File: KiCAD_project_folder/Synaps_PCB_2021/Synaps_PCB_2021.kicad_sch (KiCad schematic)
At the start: 0 parts

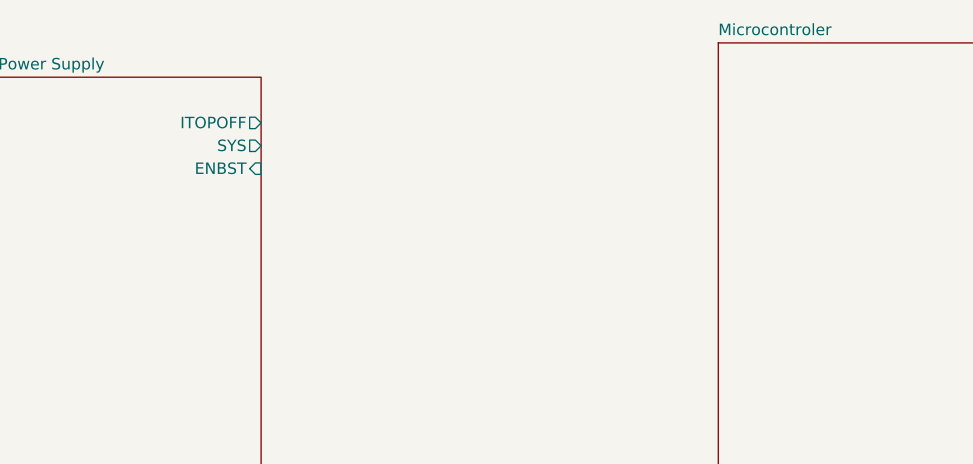
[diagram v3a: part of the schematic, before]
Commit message: Reworking Powersupply
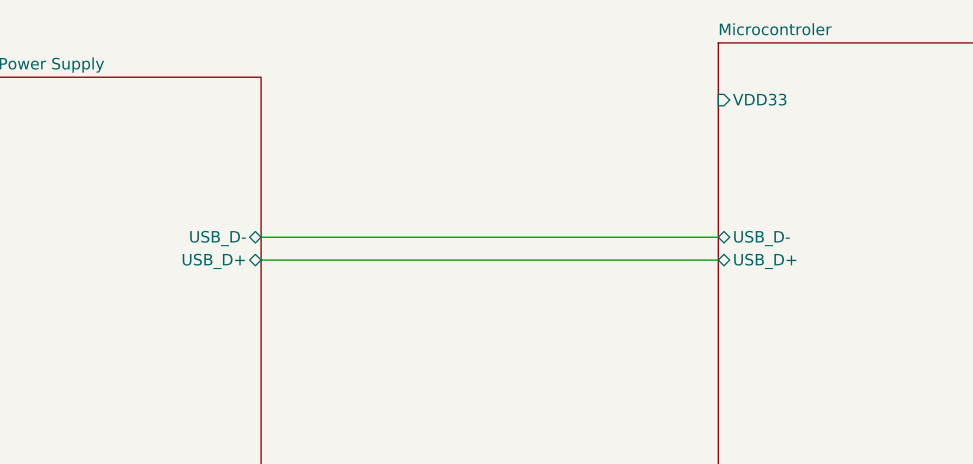
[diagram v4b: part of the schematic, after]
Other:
- sheet Microcontroler ports: added USB_D+, USB_D-, VDD33; removed none
- sheet Power Supply ports: added USB_D+, USB_D-; removed ENBST, ITOPOFF, SYS
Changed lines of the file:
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@@
     (date "2020-12-29")
+  )
+  (wire (pts (xy 76.2 62.23) (xy 127 62.23))
+    (stroke (width 0) (type default) (color 0 0 0 0))
+  )
+  (wire (pts (xy 76.2 59.69) (xy 127 59.69))
+    (stroke (width 0) (type default) (color 0 0 0 0))
   )
   (sheet (at 46.99 41.91) (size 29.21 72.39) (fields_autoplaced)
@@
       (effects (font (size 1.27 1.27)) (justify left top))
     )
-    (pin "ITOPOFF" output (at 76.2 46.99 0)
+    (pin "USB_D-" bidirectional (at 76.2 59.69 0)
       (effects (font (size 1.27 1.27)) (justify right))
     )
-    (pin "SYS" output (at 76.2 49.53 0)
-      (effects (font (size 1.27 1.27)) (justify right))
-    )
-    (pin "ENBST" input (at 76.2 52.07 0)
+    (pin "USB_D+" bidirectional (at 76.2 62.23 0)
       (effects (font (size 1.27 1.27)) (justify right))
     )
@@
     (property "Sheet file" "microcontroler.kicad_sch" (id 1) (at 127 114.8846 0)
       (effects (font (size 1.27 1.27)) (justify left top))
+    )
+    (pin "VDD33" input (at 127 44.45 180)
+      (effects (font (size 1.27 1.27)) (justify left))
+    )
+    (pin "USB_D-" bidirectional (at 127 59.69 180)
+      (effects (font (size 1.27 1.27)) (justify left))
+    )
+    (pin "USB_D+" bidirectional (at 127 62.23 180)
+      (effects (font (size 1.27 1.27)) (justify left))
     )
   )
@@
       (reference "#PWR012") (unit 1) (value "VIO") (footprint "")
     )
-    (path "/00000000-0000-0000-0000-0000604af200/ad0e8a75-3c18-4b68-b709-f2c4f54d4827"
-      (reference "#PWR013") (unit 1) (value "VIO") (footprint "")
-    )
     (path "/00000000-0000-0000-0000-0000604b51e6/00000000-0000-0000-0000-000060abb037/acdf1401-7333-43d7-ac3f-2245baffa6ea/43ac6ffa-7b63-4fc0-b2b8-4c9c5eb4bd58"
       (reference "#PWR016") (unit 1) (value "GNDREF") (footprint "")
@@
       (reference "#PWR0102") (unit 1) (value "GNDREF") (footprint "")
     )
-    (path "/00000000-0000-0000-0000-0000604af200/89827649-befc-4750-a34c-13cfb14ed735"
-      (reference "#PWR0103") (unit 1) (value "VIO") (footprint "")
-    )
     (path "/00000000-0000-0000-0000-0000604af200/29ab8ef7-d469-4192-a436-a1a2c51aa419"
       (reference "#PWR0104") (unit 1) (value "GNDREF") (footprint "")
     )
-    (path "/00000000-0000-0000-0000-0000604af200/d9362226-eaaf-4ec2-bc9f-ba927022fb72"
-      (reference "#PWR0105") (unit 1) (value "VIO") (footprint "")
-    )
-    (path "/00000000-0000-0000-0000-0000604af200/9541e854-c63a-412b-a034-49b741e570c2"
-      (reference "#PWR0106") (unit 1) (value "VIO") (footprint "")
+    (path "/00000000-0000-0000-0000-0000604af200/029525a0-8a41-486f-a02b-f13993394b49"
+      (reference "#PWR?") (unit 1) (value "GNDREF") (footprint "")
+    )
+    (path "/00000000-0000-0000-0000-0000604af200/0612be0e-3ae0-4e28-936e-756a5afc4dbe"
+      (reference "#PWR?") (unit 1) (value "+3.3V") (footprint "")
+    )
+    (path "/00000000-0000-0000-0000-0000604af200/28f76b07-ad8a-4c48-9d57-49c6c6ca56bd"
+      (reference "#PWR?") (unit 1) (value "GNDREF") (footprint "")
+    )
+    (path "/00000000-0000-0000-0000-0000604af200/4ac4cde6-c5b2-4ee8-aa21-e81b8b7c6e89"
+      (reference "#PWR?") (unit 1) (value "GNDREF") (footprint "")
+    )
+    (path "/00000000-0000-0000-0000-0000604af200/6096ff1a-efad-4c96-91e5-2b8353c01857"
+      (reference "#PWR?") (unit 1) (value "GNDREF") (footprint "")
+    )
+    (path "/00000000-0000-0000-0000-0000604af200/75e6a19c-b364-4d0b-97b2-9a6594dafad5"
+      (reference "#PWR?") (unit 1) (value "VAA") (footprint "")
+    )
+    (path "/00000000-0000-0000-0000-0000604af200/8d41ddfc-b02c-4f6e-ad73-25b463ae002b"
+      (reference "#PWR?") (unit 1) (value "GNDREF") (footprint "")
+    )
+    (path "/00000000-0000-0000-0000-0000604af200/b5aba46c-977a-4706-899d-5875980faab4"
+      (reference "#PWR?") (unit 1) (value "VDD") (footprint "")
+    )
+    (path "/00000000-0000-0000-0000-0000604af200/c3897589-3648-454c-9d3d-6573d66fd15c"
+      (reference "#PWR?") (unit 1) (value "GNDREF") (footprint "")
+    )
+    (path "/00000000-0000-0000-0000-0000604af200/e5318905-4b1b-43c9-aa4d-40970fcef07a"
+      (reference "#PWR?") (unit 1) (value "VIO") (footprint "")
+    )
+    (path "/00000000-0000-0000-0000-0000604af200/ef1da815-5ae9-4f7a-859c-d7960e6acc1e"
+      (reference "#PWR?") (unit 1) (value "VBUS") (footprint "")
     )
     (path "/00000000-0000-0000-0000-0000604b2e86/dab29796-d6b3-4d2d-805f-0b5d2109d9de"
@@
       (reference "C63") (unit 1) (value "10nF/6.3V(10%)") (footprint "Capacitor_SMD:C_1206_3216Metric_Pad1.33x1.80mm_HandSolder")
     )
+    (path "/00000000-0000-0000-0000-0000604af200/afa1e3e3-9a93-4a9d-be10-b6a15433e600"
+      (reference "C?") (unit 1) (value "0.1uF") (footprint "")
+    )
+    (path "/00000000-0000-0000-0000-0000604af200/b68089f8-3576-4418-ba7c-a83d273f4433"
+      (reference "C?") (unit 1) (value "10uF") (footprint "")
+    )
+    (path "/00000000-0000-0000-0000-0000604af200/e5285c42-bd99-4599-82cc-7692ec105054"
+      (reference "C?") (unit 1) (value "0.1uF") (footprint "")
+    )
+    (path "/00000000-0000-0000-0000-0000604af200/f6629c18-4df5-48ea-99b2-c77713f98e19"
+      (reference "C?") (unit 1) (value "10uF") (footprint "")
+    )
     (path "/00000000-0000-0000-0000-0000604af200/5213bc81-6974-4343-aba7-970b9f36c652"
       (reference "D2") (unit 1) (value "LED") (footprint "LED_SMD:LED_1206_3216Metric_Pad1.42x1.75mm_HandSolder")
@@
       (reference "L4") (unit 1) (value "INDUCTOR") (footprint "Inductor_SMD:L_1206_3216Metric_Pad1.22x1.90mm_HandSolder")
     )
+    (path "/00000000-0000-0000-0000-0000604af200/9d05efa6-c335-40cb-8451-b925832a8438"
+      (reference "L?") (unit 1) (value "L_Ferrite") (footprint "")
+    )
     (path "/00000000-0000-0000-0000-0000604af200/30e58f79-c173-4870-9af4-7e80c241c783"
       (reference "Q2") (unit 1) (value "Q_PMOS_DGS") (footprint "")
@@
       (reference "R2") (unit 1) (value "10K") (footprint "Resistor_SMD:R_1206_3216Metric_Pad1.30x1.75mm_HandSolder")
     )
-    (path "/00000000-0000-0000-0000-0000604af200/6f377bca-1c7b-4d57-a89d-9e25d90f18a5"
-      (reference "R3") (unit 1) (value "4.7K") (footprint "Resistor_SMD:R_1206_3216Metric_Pad1.30x1.75mm_HandSolder")
-    )
-    (path "/00000000-0000-0000-0000-0000604af200/c8d586cf-013f-4922-a958-a02f8fecd9fa"
-      (reference "R4") (unit 1) (value "4.7K") (footprint "Resistor_SMD:R_1206_3216Metric_Pad1.30x1.75mm_HandSolder")
-    )
     (path "/00000000-0000-0000-0000-0000604af200/8192b8bb-5861-4b6a-a2f5-d5f4d61eff20"
       (reference "R5") (unit 1) (value "4.7K") (footprint "Resistor_SMD:R_1206_3216Metric_Pad1.30x1.75mm_HandSolder")
@@
       (reference "R12") (unit 1) (value "4.7K") (footprint "Resistor_SMD:R_1206_3216Metric_Pad1.30x1.75mm_HandSolder")
     )
+    (path "/00000000-0000-0000-0000-0000604af200/0db8a049-a6a2-4724-ac1c-20b36cc3d210"
+      (reference "R?") (unit 1) (value "1M") (footprint "")
+    )
+    (path "/00000000-0000-0000-0000-0000604af200/d0d129c1-fb34-4572-a9d4-1007e110f1d8"
+      (reference "R?") (unit 1) (value "4.7K") (footprint "Resistor_SMD:R_1206_3216Metric_Pad1.30x1.75mm_HandSolder")
+    )
     (path "/00000000-0000-0000-0000-0000604af200/13c63bdd-8124-498f-a41a-0d57f55b9907"

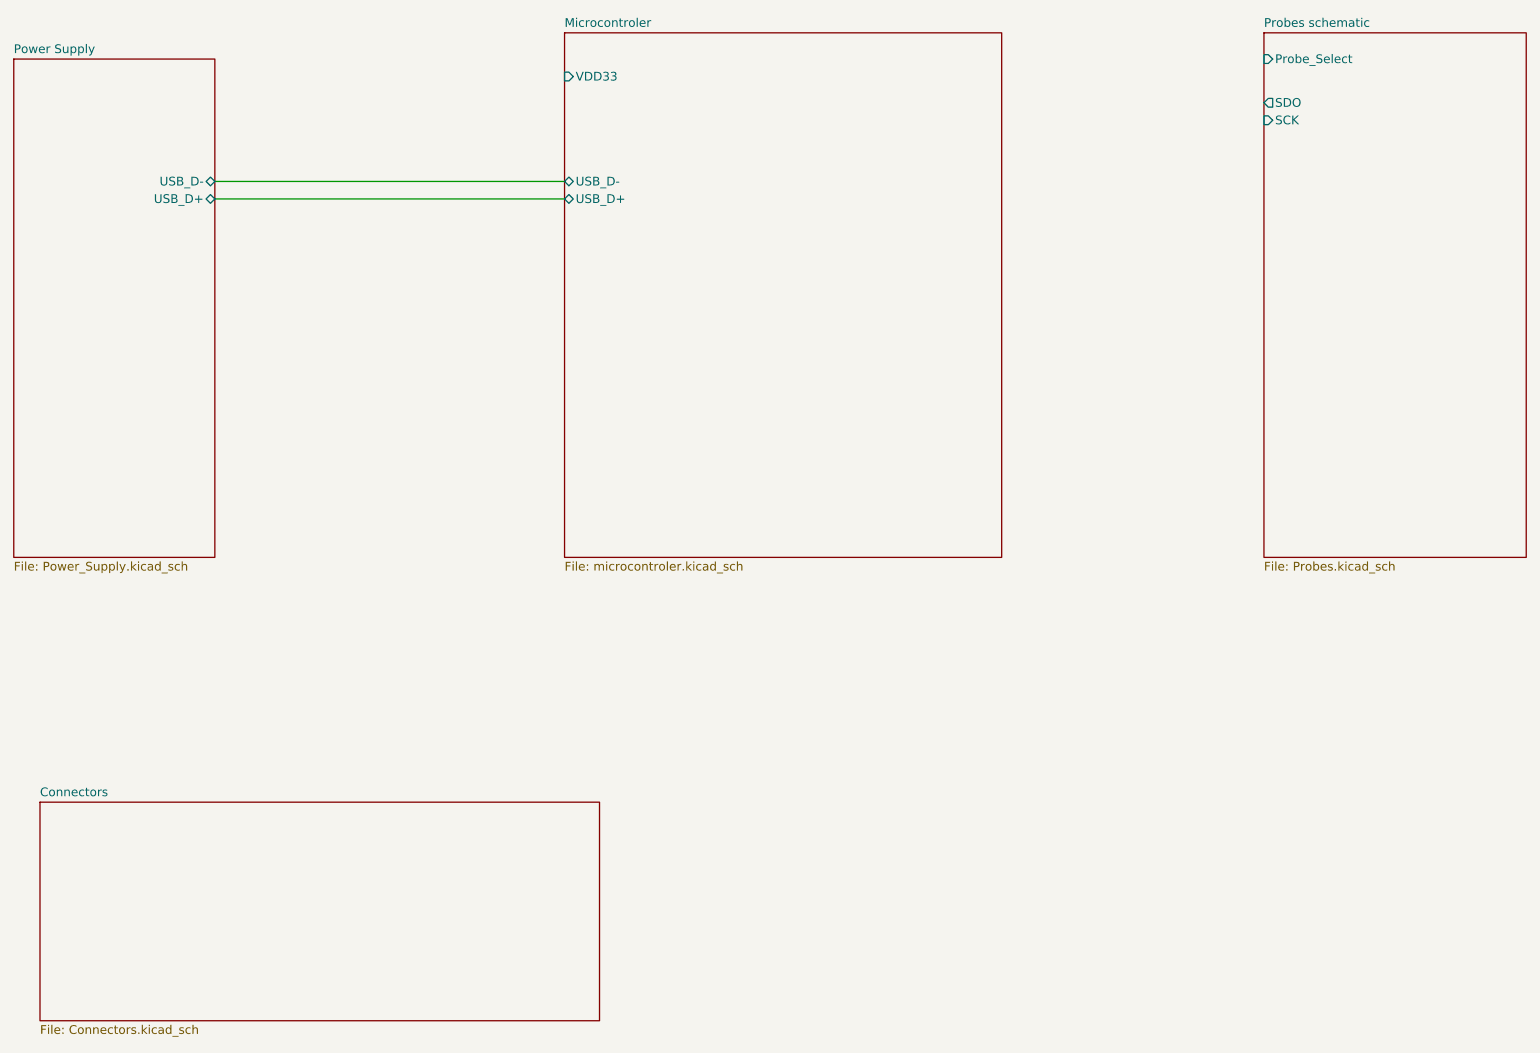
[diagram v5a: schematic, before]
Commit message: Reworded PMIC and probe select
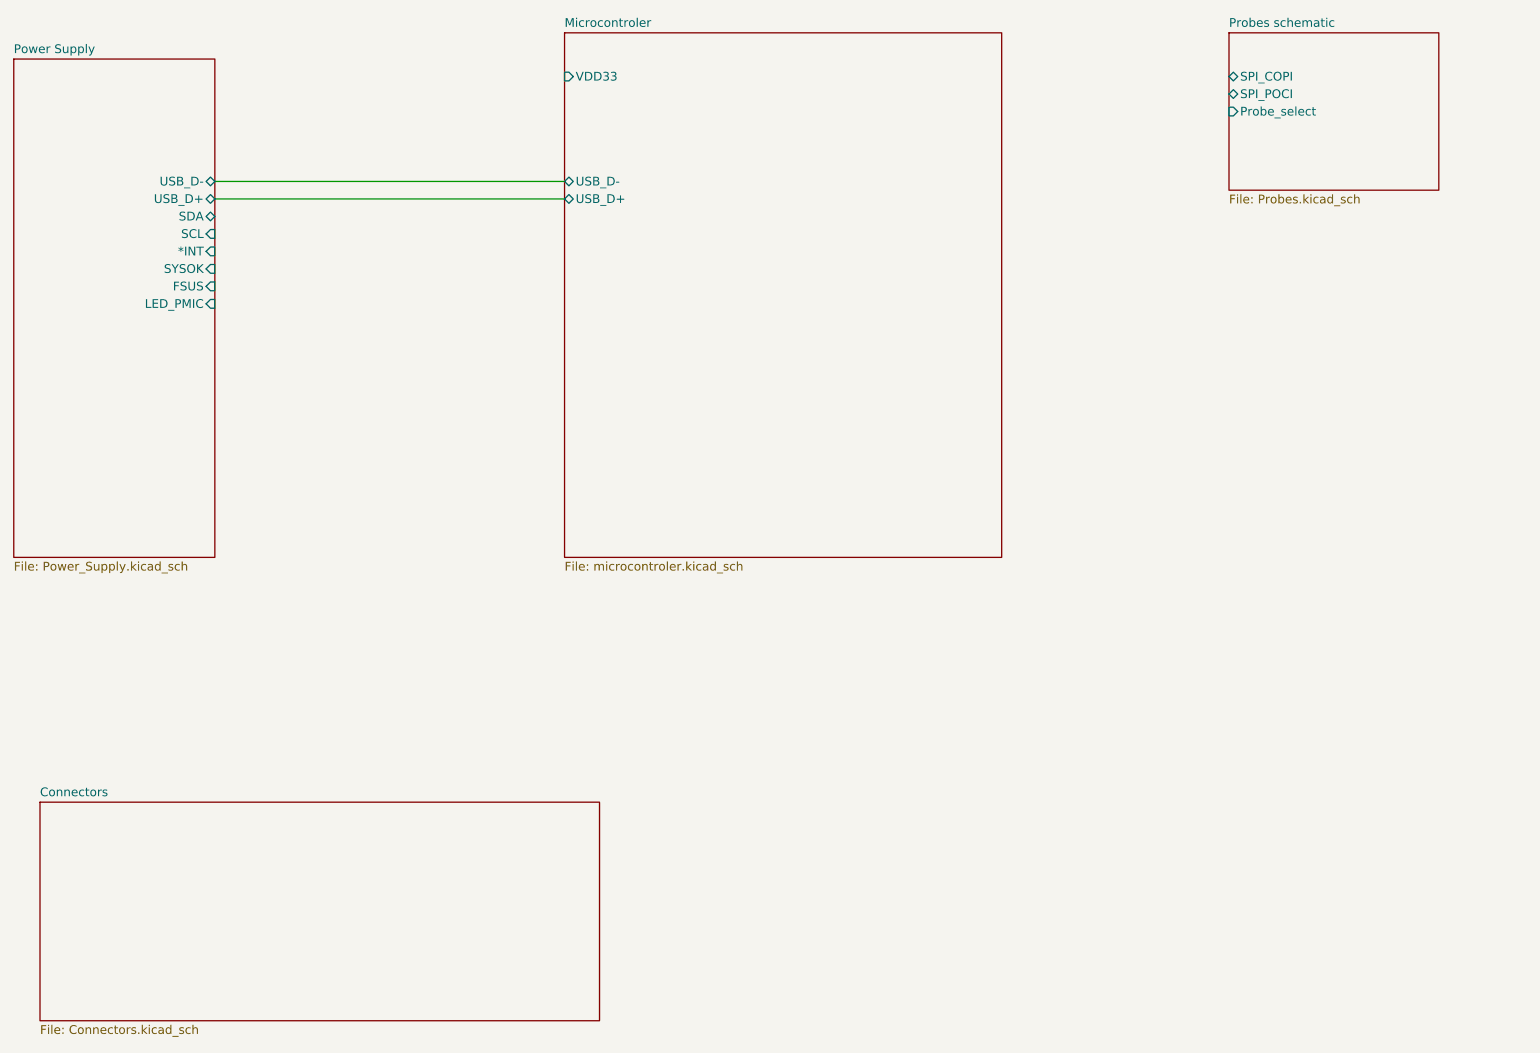
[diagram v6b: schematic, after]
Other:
- sheet Power Supply ports: added *INT, FSUS, LED_PMIC, SCL, SDA, SYSOK; removed none
- sheet Probes schematic ports: added Probe_select, SPI_COPI, SPI_POCI; removed Probe_Select, SCK, SDO

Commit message: Redid schematic, fixed wrong setup
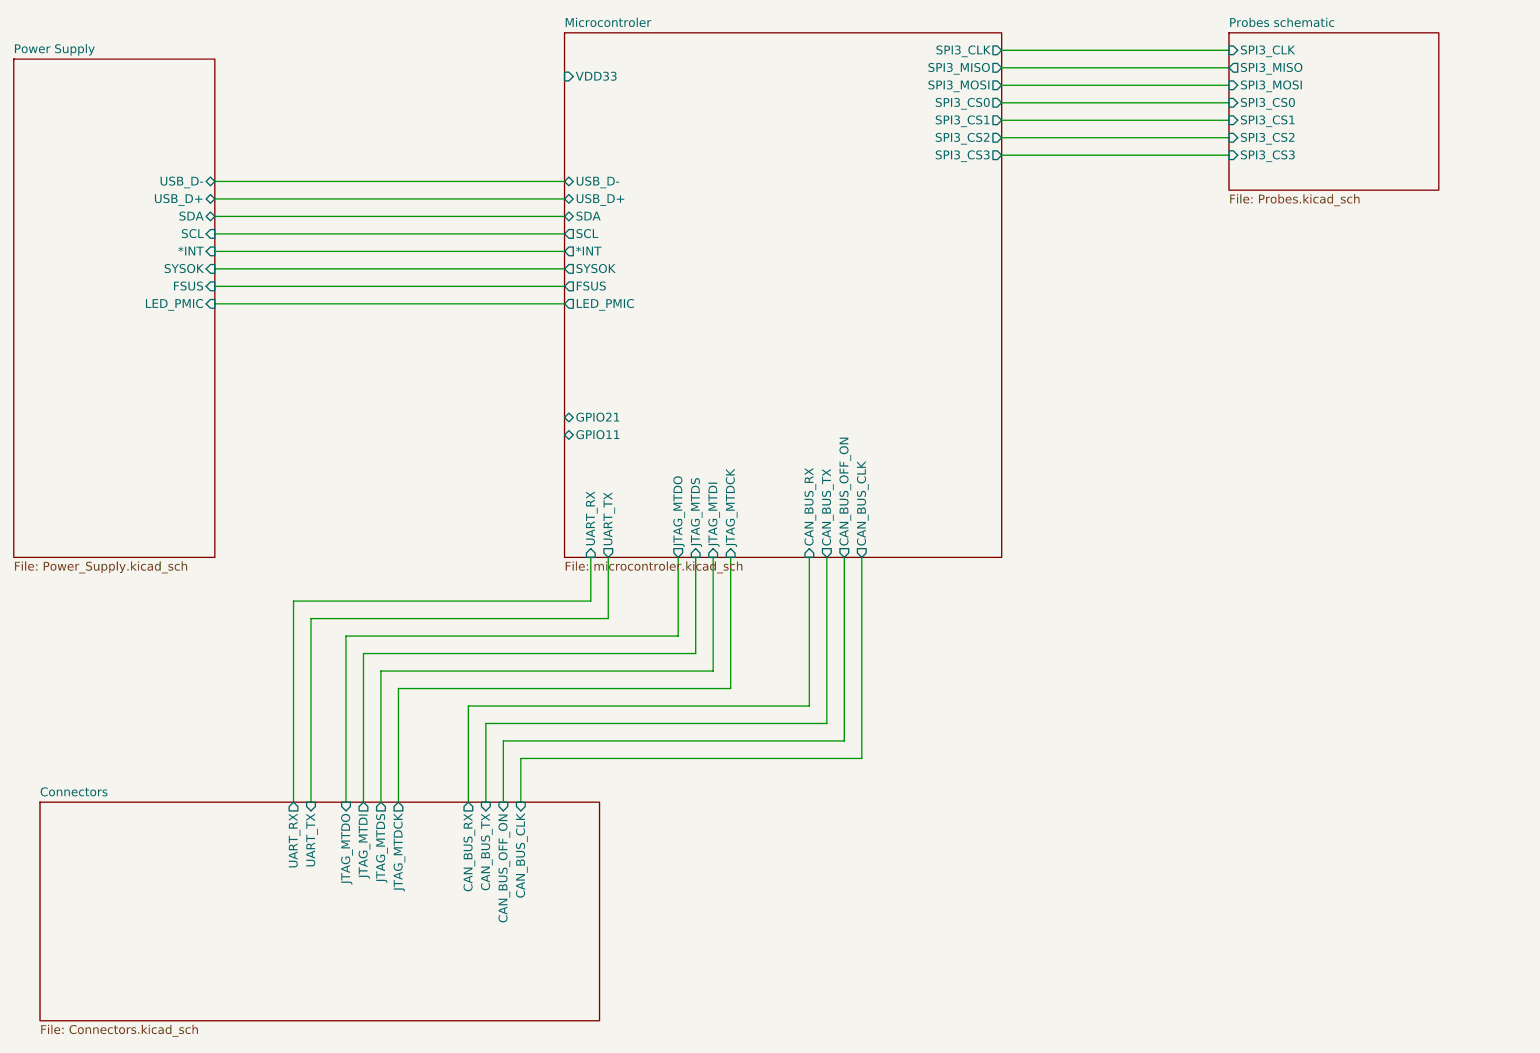
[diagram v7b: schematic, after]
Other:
- sheet Connectors ports: added CAN_BUS_CLK, CAN_BUS_OFF_ON, CAN_BUS_RX, CAN_BUS_TX, JTAG_MTDCK, JTAG_MTDI, JTAG_MTDO, JTAG_MTDS, UART_RX, UART_TX; removed none
- sheet Microcontroler ports: added *INT, CAN_BUS_CLK, CAN_BUS_OFF_ON, CAN_BUS_RX, CAN_BUS_TX, FSUS, GPIO11, GPIO21, JTAG_MTDCK, JTAG_MTDI, JTAG_MTDO, JTAG_MTDS, LED_PMIC, SCL, SDA, SPI3_CLK, SPI3_CS0, SPI3_CS1, SPI3_CS2, SPI3_CS3, SPI3_MISO, SPI3_MOSI, SYSOK, UART_RX, UART_TX; removed none
- sheet Probes schematic ports: added SPI3_CLK, SPI3_CS0, SPI3_CS1, SPI3_CS2, SPI3_CS3, SPI3_MISO, SPI3_MOSI; removed Probe_select, SPI_COPI, SPI_POCI
